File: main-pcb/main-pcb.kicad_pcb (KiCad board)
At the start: 10 copper layers, 118 x 90 mm, 443 parts, among them J1 CONN_01X03, J10 CONN_DUMPTRUCK_HOST, J11 CONN_01X03, J12 PMOD_HOST, J13 PMOD_HOST, J14 USB_C_Receptacle_USB2.0, J2 CORTEX_DEBUG_ETM, J3 XILINX_JTAG, J4 CORTEX_DEBUG_ETM, J5 CONN_01X03, J6 0826-1G1T-23-F, J7 CONN_DUMPTRUCK_HOST, J8 CONN_DUMPTRUCK_HOST, J9 CONN_DUMPTRUCK_HOST, M1 MECHANICAL, M2 SCREWHOLE, M3 SCREWHOLE, M4 SCREWHOLE, M5 SCREWHOLE, M6 MECHANICAL, M7 MECHANICAL, M8 MECHANICAL, M9 MECHANICAL, Q1 SSM6N58NU, SW1 SWITCH, SW2 SWITCH, U1 XC7S100-1FGGA484C, U10 NCP45525IMNTWG-H, U11 LTC3374-QFN, U12 AT24MAC402, U13 ECS-1612MV-250-CN, U14 STM32H735-UFBGA176-25, U15 S27KL0642GABHB020, U16 ECS-1612MV-250-CN, U17 S27KS0642GABHI030, U18 ECS-1612MV-250-CN, U19 INA230, U2 STM32L431-QFN48, U20 KSZ9031RN, U21 RCLAMP0514M, U22 RCLAMP0514M, U23 NCP45525IMNTWG-H, U24 IS25WP256D-JLLE, U25 INA230, U26 74LVC1T45, U27 NCP45525IMNTWG-H, U28 INA230, U29 NCP45525IMNTWG-H, U3 INA230, U30 INA230, U31 NCP45525IMNTWG-H, U32 INA230, U33 19-C47/RSGHBHC-5V01/2T, U34 19-C47/RSGHBHC-5V01/2T, U35 19-C47/RSGHBHC-5V01/2T, U36 19-C47/RSGHBHC-5V01/2T, U37 19-C47/RSGHBHC-5V01/2T, U38 19-C47/RSGHBHC-5V01/2T, U39 NCP45525IMNTWG-H, U4 INA230, U5 INA230, U6 INA230, U7 INA230, U8 INA230, U9 INA230

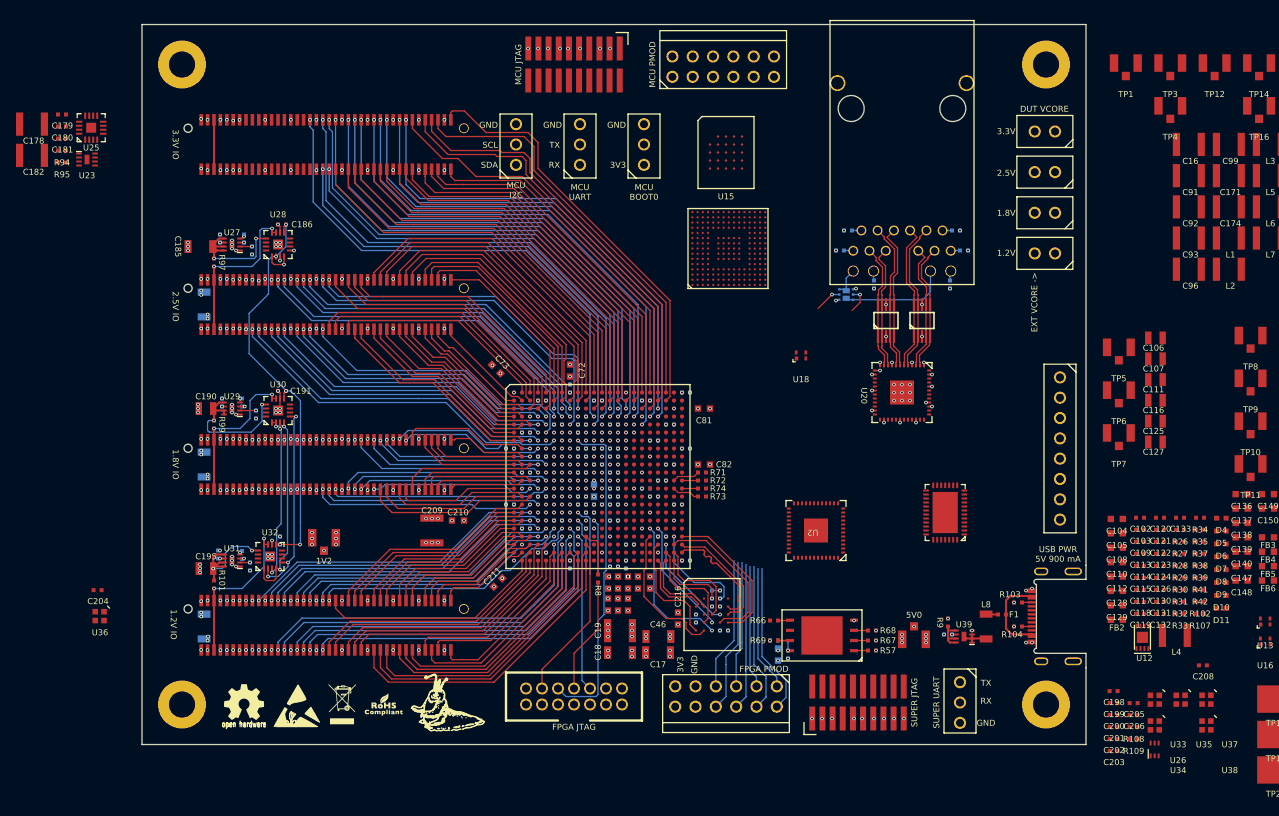
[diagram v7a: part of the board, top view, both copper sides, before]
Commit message: Started work on main CPU routing
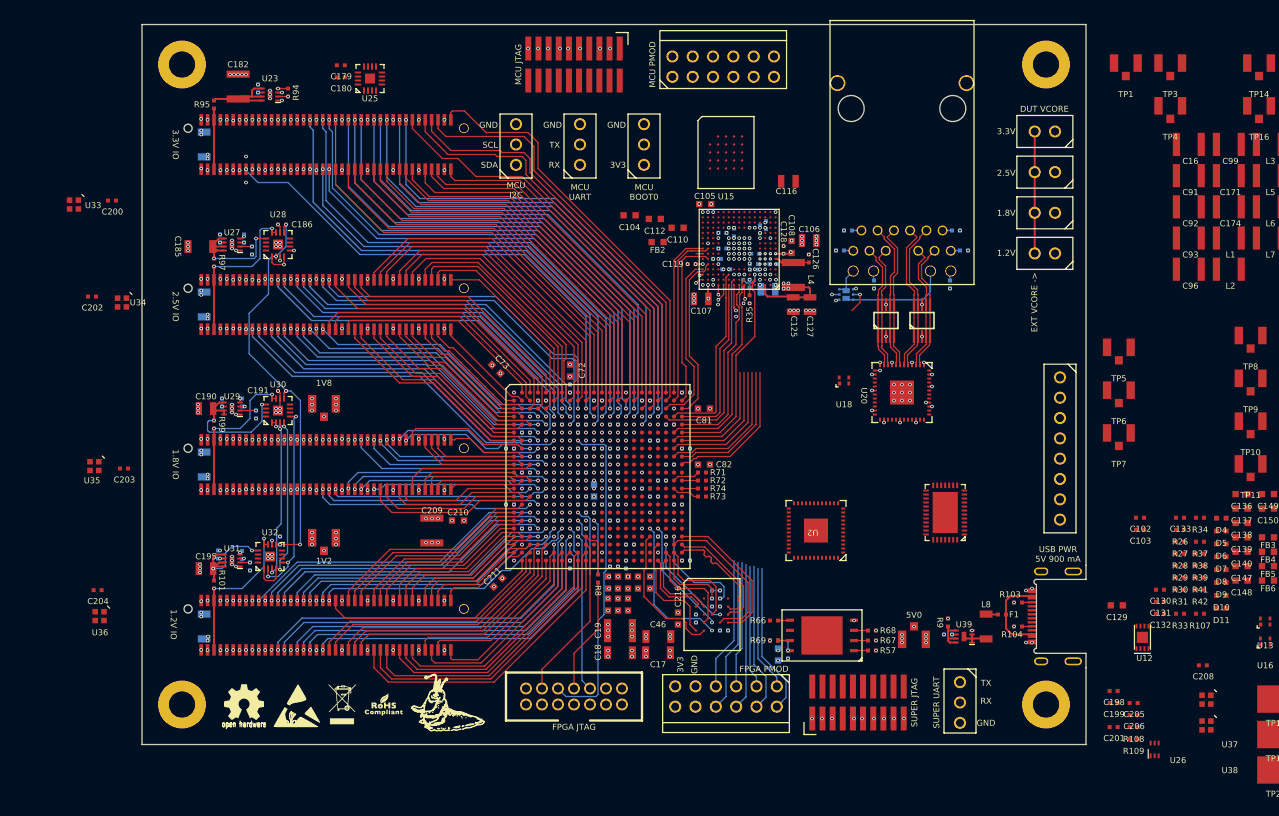
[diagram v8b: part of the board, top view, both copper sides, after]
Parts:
- C109: value 0.1 uF -> 0.47 uF; moved to B.Cu
- C111, C113, C114, C115, C117, C118, C120, C121, C122, C123, C124, C181, R102, R32: moved to B.Cu
- C128: footprint azonenberg_pcb:EIA_0603_CAP_NOSILK -> azonenberg_pcb:EIA_0402_CAP_NOSILK
- C178: footprint azonenberg_pcb:EIA_1210_CAP_NOSILK -> azonenberg_pcb:EIA_1206_CAP_NOSILK; moved to B.Cu
- moved U33 148.6 mm to (28.5, 48.5)
- moved C200 140.8 mm to (33.2, 48.0)
- moved U34 139.5 mm to (34.5, 60.8)
- moved C202 139.2 mm to (30.8, 60.0)
- moved U35 138.9 mm to (31.1, 81.2)
- moved C203 128.6 mm to (34.8, 81.5)
- moved TP12 119.2 mm to (59.8, 73.5)
- moved FB2 74.3 mm to (101.5, 53.2)
- moved C112 73.0 mm to (101.1, 50.3)
- moved C104 71.8 mm to (98.0, 49.9)
- moved C119 71.1 mm to (105.7, 56.0), turned to 180 degrees
- moved R102 69.6 mm to (112.2, 58.4), turned to -90 degrees
- moved C110 69.0 mm to (104.0, 51.4)
- moved C118 68.6 mm to (111.0, 52.0), turned to 90 degrees
- moved R32 66.9 mm to (113.0, 58.4), turned to 90 degrees
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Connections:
- U1 pad A21: /MCU/FMC_CLK -> /MCU/FMC_A18
- U1 pad B21: /MCU/FMC_AD2 -> /MCU/FMC_AD0
- U1 pad B22: /MCU/FMC_AD3 -> /MCU/FMC_NE3
- U1 pad C10: /3V3 VCCIO socket/DUT_GPIO5 -> /3V3 VCCIO socket/DUT_GPIO1
- U1 pad C20: /MCU/FMC_AD5 -> /MCU/FMC_NE1
- U1 pad C22: /MCU/FMC_AD7 -> /MCU/FMC_NWAIT
- U1 pad D20: /MCU/FMC_AD4 -> /MCU/FMC_NWE
- U1 pad D21: /MCU/FMC_AD6 -> /MCU/FMC_AD2
- U1 pad D22: /MCU/FMC_AD9 -> /MCU/FMC_AD3
- U1 pad E12: /3V3 VCCIO socket/DUT_GPIO10 -> /3V3 VCCIO socket/DUT_GPIO7
- U1 pad E15: /3V3 VCCIO socket/DUT_GPIO15 -> /3V3 VCCIO socket/DUT_GPIO6
- U1 pad E16: /3V3 VCCIO socket/DUT_GPIO14 -> /3V3 VCCIO socket/DUT_GPIO10
- U1 pad E18: /3V3 VCCIO socket/DUT_GPIO6 -> /3V3 VCCIO socket/DUT_GPIO12
- U1 pad E19: /3V3 VCCIO socket/DUT_GPIO13 -> /3V3 VCCIO socket/DUT_GPIO14
- U1 pad E22: /MCU/FMC_AD8 -> /MCU/FMC_NE2
- U1 pad F10: /3V3 VCCIO socket/DUT_GPIO4 -> /3V3 VCCIO socket/DUT_GPIO3
- U1 pad F11: /3V3 VCCIO socket/DUT_GPIO2 -> /3V3 VCCIO socket/DUT_GPIO5
- U1 pad F12: /3V3 VCCIO socket/DUT_GPIO9 -> /3V3 VCCIO socket/DUT_GPIO4
- U1 pad F13: /3V3 VCCIO socket/DUT_GPIO7 -> /3V3 VCCIO socket/DUT_GPIO11
- U1 pad F14: /3V3 VCCIO socket/DUT_GPIO8 -> /3V3 VCCIO socket/DUT_GPIO15
- U1 pad F15: /3V3 VCCIO socket/DUT_GPIO12 -> /3V3 VCCIO socket/DUT_GPIO17
- U1 pad F17: /MCU/FMC_NWAIT -> /MCU/FMC_AD7
- U1 pad F19: /MCU/FMC_AD12 -> /MCU/FMC_CLK
- U1 pad F21: /MCU/FMC_AD10 -> /MCU/FMC_A24
- U1 pad F22: /MCU/FMC_AD11 -> /MCU/FMC_NL_NADV
- U1 pad G10: /3V3 VCCIO socket/DUT_GPIO3 -> /3V3 VCCIO socket/DUT_GPIO0
- U1 pad G11: /3V3 VCCIO socket/DUT_GPIO1 -> /3V3 VCCIO socket/DUT_GPIO2
- U1 pad G13: /3V3 VCCIO socket/DUT_GPIO0 -> /3V3 VCCIO socket/DUT_GPIO9
- U1 pad G14: /3V3 VCCIO socket/DUT_GPIO11 -> /3V3 VCCIO socket/DUT_GPIO13
- U1 pad G15: /3V3 VCCIO socket/DUT_GPIO17 -> /3V3 VCCIO socket/DUT_GPIO8
- U1 pad G16: /MCU/FMC_NE2 -> /MCU/FMC_AD8
- U1 pad G21: /MCU/FPGA_LED_0 -> /MCU/FMC_A17
- U1 pad G22: /MCU/FPGA_LED_1 -> /MCU/FMC_AD9
- U1 pad H16: /MCU/FMC_NE1 -> /MCU/FMC_AD5
- U1 pad H17: /MCU/FMC_NWE -> /MCU/FMC_AD4
- U1 pad H18: /MCU/FMC_NL_NADV -> /MCU/FMC_AD11
- U1 pad H19: /MCU/FMC_A24 -> /MCU/FMC_AD10
- U1 pad H20: /MCU/FPGA_LED_2 -> /MCU/FMC_AD14
- U1 pad H21: /MCU/FPGA_LED_3 -> /MCU/FMC_AD15
- U1 pad J16: /LED_CTRL -> /MCU/FMC_A19
- U1 pad J21: /MCU/FPGA_PMOD_DQ2 -> /MCU/FMC_A22
- U1 pad J22: /MCU/FPGA_PMOD_DQ3 -> /MCU/FMC_A23
- U1 pad K15: /MCU/FMC_AD0 -> /LED_CTRL
- U1 pad K16: /MCU/FMC_NE3 -> /MCU/FPGA_PMOD_DQ1
- U1 pad K17: /MCU/FMC_A17 -> /MCU/FPGA_LED_2
- U1 pad K18: /MCU/FMC_A18 -> /MCU/FMC_AD12
- U1 pad K19: /MCU/FMC_A19 -> /MCU/FMC_AD6
- U1 pad K22: /MCU/FPGA_PMOD_DQ1 -> /MCU/FMC_A16
- U1 pad L16: /MCU/FMC_A16 -> /MCU/FPGA_LED_3
- U1 pad L18: /MCU/FMC_A22 -> /MCU/FPGA_PMOD_DQ2
- U1 pad L19: /MCU/FMC_A23 -> /MCU/FPGA_PMOD_DQ3
- U1 pad M17: /MCU/FMC_AD14 -> /MCU/FPGA_LED_0
- U1 pad M18: /MCU/FMC_AD15 -> /MCU/FPGA_LED_1
- U14 pad B10: /MCU/MCU_PMOD_DQ1 -> unconnected-(U14D-PD2-PadB10)
- U14 pad D14: /MCU/MCU_PMOD_DQ2 -> unconnected-(U14C-PC8-PadD14)
- U14 pad M15: unconnected-(U14B-PB12-PadM15) -> /MCU/MCU_PMOD_DQ2
- U14 pad R10: unconnected-(U14F-PF14-PadR10) -> /MCU/MCU_PMOD_DQ1
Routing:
- net /DUT_VDD: track 68.2 -> 171.9 mm, vias 14 -> 16
- net /GND: track 1212.7 -> 1304.7 mm, vias 309 -> 388
- net /3V3: track 253.1 -> 323.8 mm, vias 19 -> 45
- net /3V3 VCCIO socket/DUT_GPIO6: track 0.00 -> 68.4 mm, vias 0 -> 2
- net /3V3 VCCIO socket/DUT_GPIO2: track 4.57 -> 70.5 mm, vias 1 -> 2
- net /3V3 VCCIO socket/DUT_GPIO4: track 4.18 -> 69.7 mm, vias 1 -> 2
- net /3V3 VCCIO socket/DUT_GPIO8: track 5.13 -> 70.0 mm, vias 1 -> 2
- net /3V3 VCCIO socket/DUT_GPIO0: track 6.25 -> 70.9 mm, vias 1 -> 2
- net /3V3 VCCIO socket/DUT_GPIO10: track 3.83 -> 68.1 mm, vias 1 -> 2
- net /3V3 VCCIO socket/DUT_GPIO5: track 0.00 -> 63.4 mm, vias 0 -> 2
- net /3V3 VCCIO socket/DUT_GPIO14: track 4.77 -> 67.6 mm, vias 1 -> 2
- net /3V3 VCCIO socket/DUT_GPIO13: track 0.00 -> 62.6 mm, vias 0 -> 2
- net /3V3 VCCIO socket/DUT_GPIO12: track 5.85 -> 67.5 mm, vias 1 -> 2
- net /3V3 VCCIO socket/DUT_GPIO9: track 5.15 -> 63.7 mm, vias 1 -> 2
- net /3V3 VCCIO socket/DUT_GPIO3: track 5.23 -> 63.1 mm, vias 1 -> 2
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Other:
- board text added: "1V8"
